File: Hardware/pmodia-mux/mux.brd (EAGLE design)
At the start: 30.5 x 8.7 mm, 17 parts, among them X2 FH12-16S-0.5SH

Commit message: Updates
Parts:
- U$8, U$9: device pad:PAD -> padLarge:PAD
- moved U$7 5.89 mm to (29.9, 3.59)
- moved U$6 5.19 mm to (30.1, 3.09)
- moved U$5 4.49 mm to (30.3, 2.60)
- moved U$4 3.63 mm to (30.5, 2.10)
- moved U$8 3.53 mm to (26.6, 3.93)
- moved U$3 3.06 mm to (30.7, 1.60)
- moved U$9 2.62 mm to (26.6, 4.67)
- moved U$10 2.60 mm to (29.9, 5.09)
- moved U$2 2.39 mm to (30.9, 1.10)
- moved U$11 2.37 mm to (30.1, 5.59)
- moved U$12 2.15 mm to (30.3, 6.09)
- moved U$13 1.95 mm to (30.5, 6.59)
- moved U$14 1.76 mm to (30.7, 7.09)
- moved U$1 1.73 mm to (31.1, 0.60)
- moved U$15 1.60 mm to (30.9, 7.59)
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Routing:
- net N$10: track 0.00 -> 28.6 mm
- net N$9: track 0.00 -> 25.1 mm
- net N$8: track 0.00 -> 25.1 mm
- net N$1: track 1.06 -> 0.00 mm
- net N$15: track 0.86 -> 0.00 mm
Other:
- board size 30.5 x 8.7 mm -> 32 x 9.3 mm

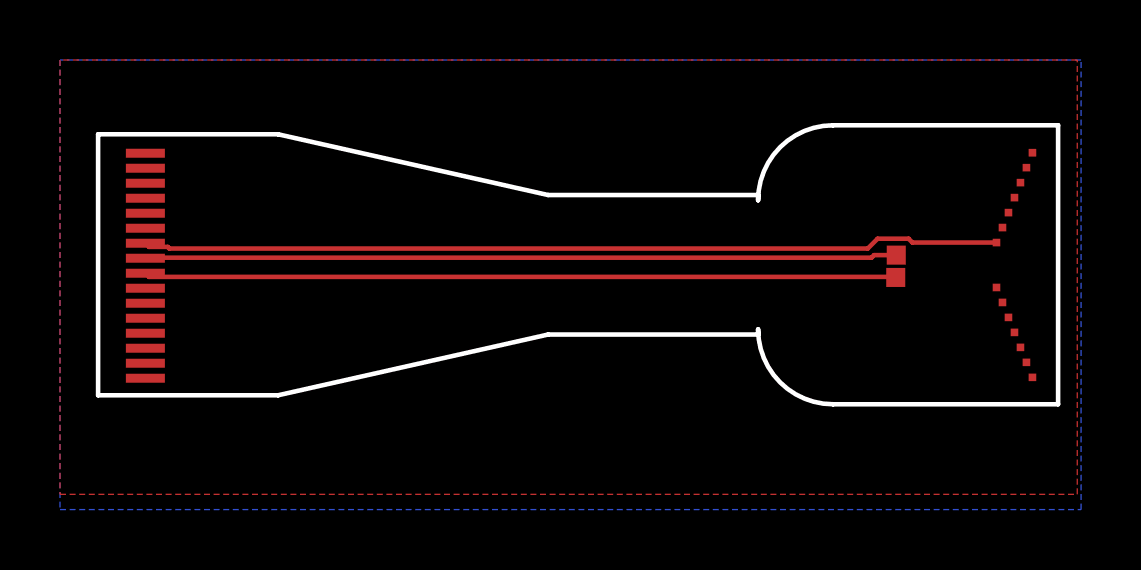
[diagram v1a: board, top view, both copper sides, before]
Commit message: Finished Flex PCB
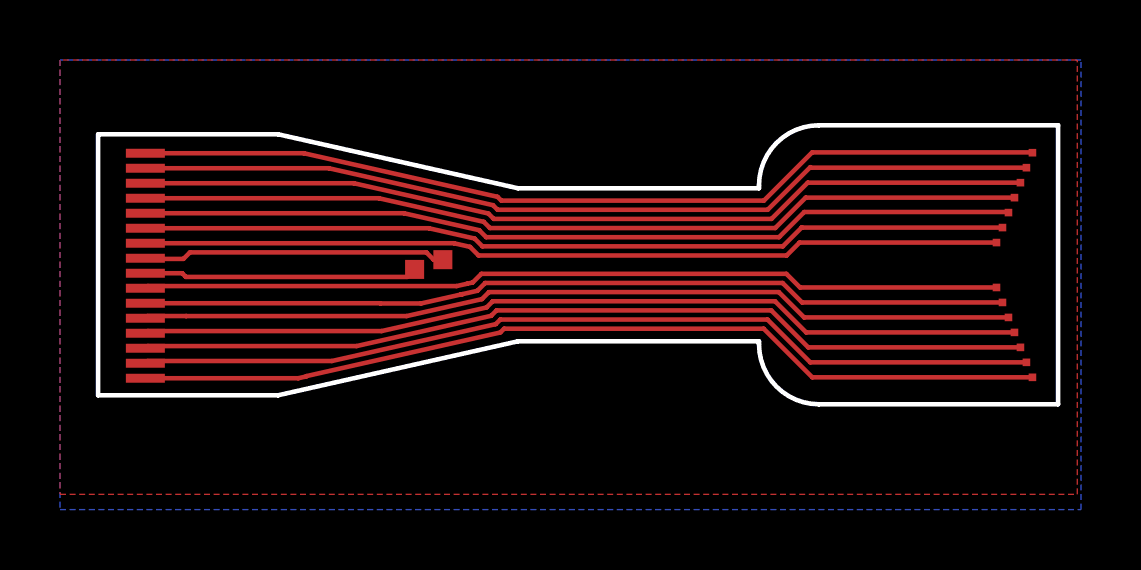
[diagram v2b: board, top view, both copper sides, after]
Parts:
- moved U$8 16.0 mm to (10.6, 4.20)
- moved U$9 15.1 mm to (11.5, 4.52)
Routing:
- net N$1: track 0.00 -> 30.5 mm
- net N$16: track 0.00 -> 30.5 mm
- net N$2: track 0.00 -> 30.2 mm
- net N$15: track 0.00 -> 30.2 mm
- net N$3: track 0.00 -> 29.9 mm
- net N$14: track 0.00 -> 29.9 mm
- net N$4: track 0.00 -> 29.6 mm
- net N$13: track 0.00 -> 29.6 mm
- net N$5: track 0.00 -> 29.3 mm
- net N$12: track 0.00 -> 29.3 mm
- net N$6: track 0.00 -> 29.1 mm
- net N$11: track 0.00 -> 29.0 mm
- net N$7: track 0.00 -> 28.7 mm
- net N$8: track 25.1 -> 9.13 mm
- net N$9: track 25.1 -> 10.1 mm
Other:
- outline, holes or cut-outs redrawn

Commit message: Updates
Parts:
- moved X2 0.55 mm to (4.28, 4.33)
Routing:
- net N$6: track 29.1 -> 29.6 mm
- net N$8: track 9.13 -> 9.68 mm
- net N$9: track 10.1 -> 10.7 mm
- net N$12: track 29.3 -> 29.8 mm
- net N$11: track 29.0 -> 29.5 mm
- net N$10: track 28.7 -> 29.2 mm
- net N$15: track 30.2 -> 30.7 mm
- net N$14: track 29.9 -> 30.4 mm
- net N$13: track 29.6 -> 30.1 mm
- net N$16: track 30.5 -> 31.0 mm
- net N$1: track 30.5 -> 31.0 mm
- net N$7: track 28.7 -> 29.3 mm
- net N$5: track 29.3 -> 29.9 mm
- net N$4: track 29.6 -> 30.1 mm
- net N$3: track 29.9 -> 30.4 mm
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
